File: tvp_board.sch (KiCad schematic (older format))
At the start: 59 parts, among them U1 TVP7002PZP, U4 SN74LVC2G17, U5 AP7361C, U6 TLV70033, U7 NCP703SN19T1G, U9 TLV70019, X1 ACHL-27MHZ-EK, X2 ASEDV-27.000MHZ-LR-T(ECS-2333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

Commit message: update PCB
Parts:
- added D4: RB160M-30TR, custom_components:D_SOD-123_HandSoldering, symbol Device:D_Schottky_ALT
- U5: value AP7361C -> BD33FC0FP; footprint custom_components:SOT-223_Handsoldering -> Package_TO_SOT_SMD:TO-252-2
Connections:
- wire segments 199 -> 203
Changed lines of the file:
@@
 P 10250 3950
 F 0 "U5" H 10250 4200 40  0000 C CNN
-F 1 "AP7361C" H 10250 4150 40  0000 C CNN
-F 2 "custom_components:SOT-223_Handsoldering" H 10250 4050 35  0001 C CIN
+F 1 "BD33FC0FP" H 10250 4150 40  0000 C CNN
+F 2 "Package_TO_SOT_SMD:TO-252-2" H 10250 4050 35  0001 C CIN
 F 3 "" H 10250 3950 60  0000 C CNN
 	1    10250 3950
@@
 	1    0    0    1
 $EndComp
+$Comp
+L Device:D_Schottky_ALT D4
+U 1 1 5FD59D9B
+P 10450 3600
+F 0 "D4" H 10450 3816 50  0000 C CNN
+F 1 "RB160M-30TR" H 10450 3725 50  0000 C CNN
+F 2 "custom_components:D_SOD-123_HandSoldering" H 10450 3600 50  0001 C CNN
+F 3 "~" H 10450 3600 50  0001 C CNN
+	1    10450 3600
+	1    0    0    -1
+$EndComp
+Wire Wire Line
+	10800 3900 10800 3600
+Wire Wire Line
+	10800 3600 10600 3600
+Wire Wire Line
+	10300 3600 9650 3600
+Wire Wire Line
+	9650 3600 9650 3900
 $EndSCHEMATC

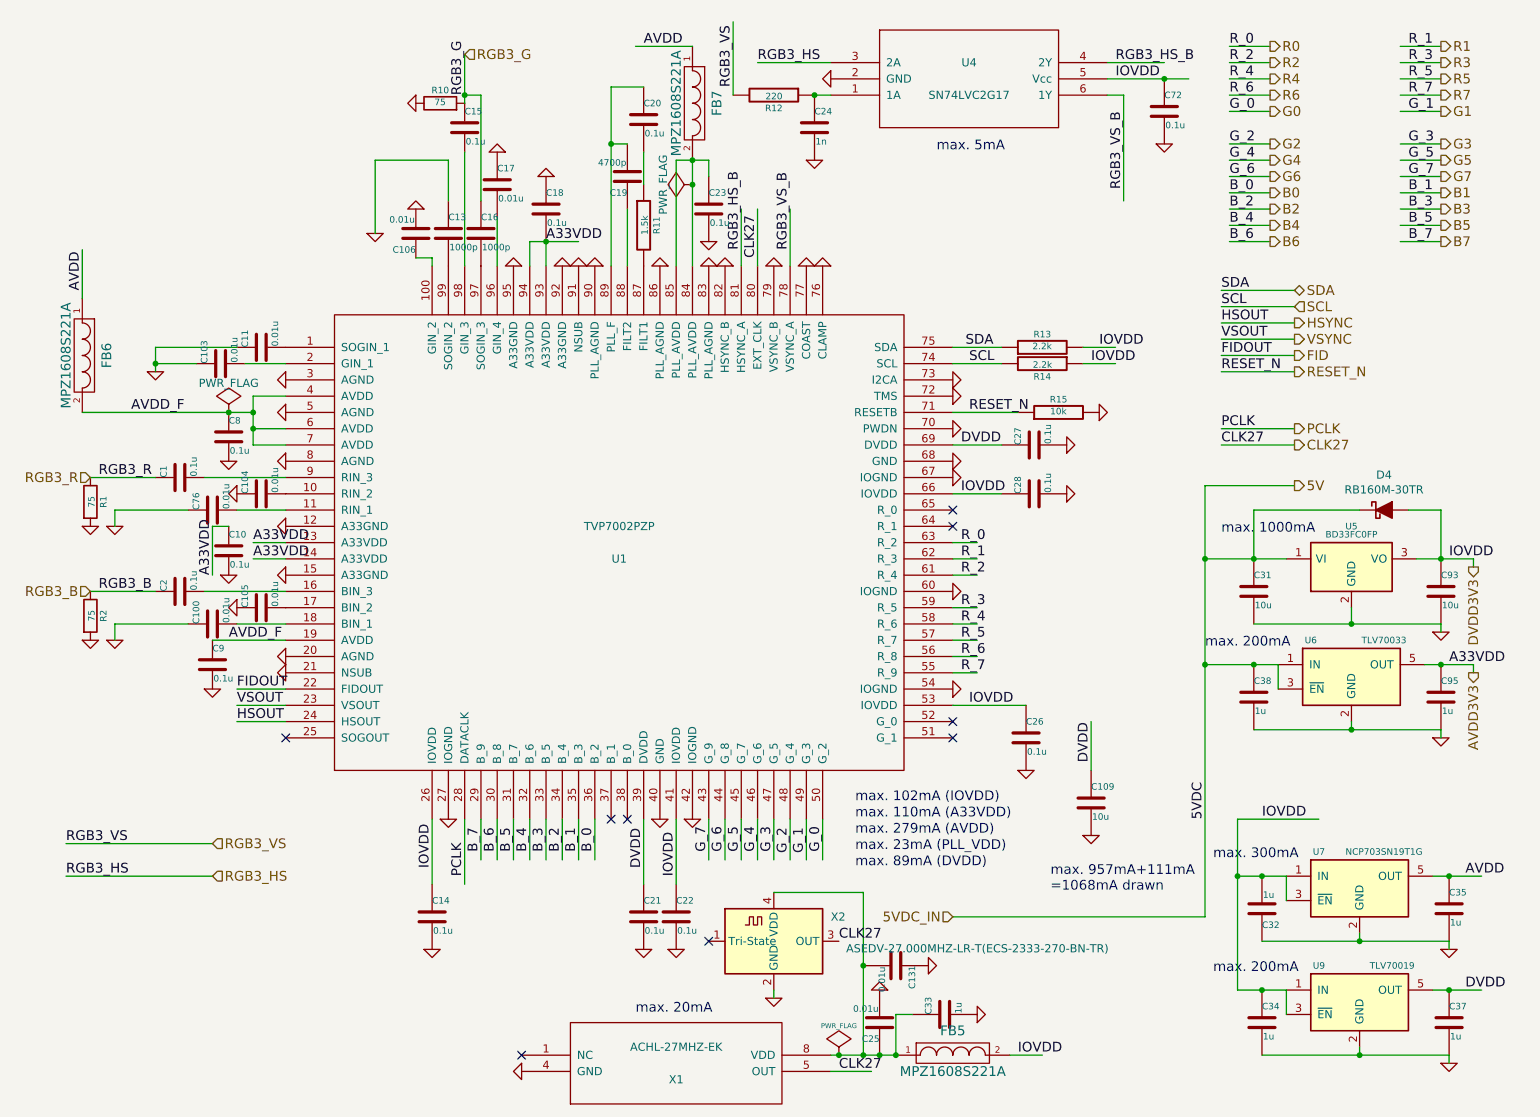
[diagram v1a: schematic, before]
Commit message: update part no
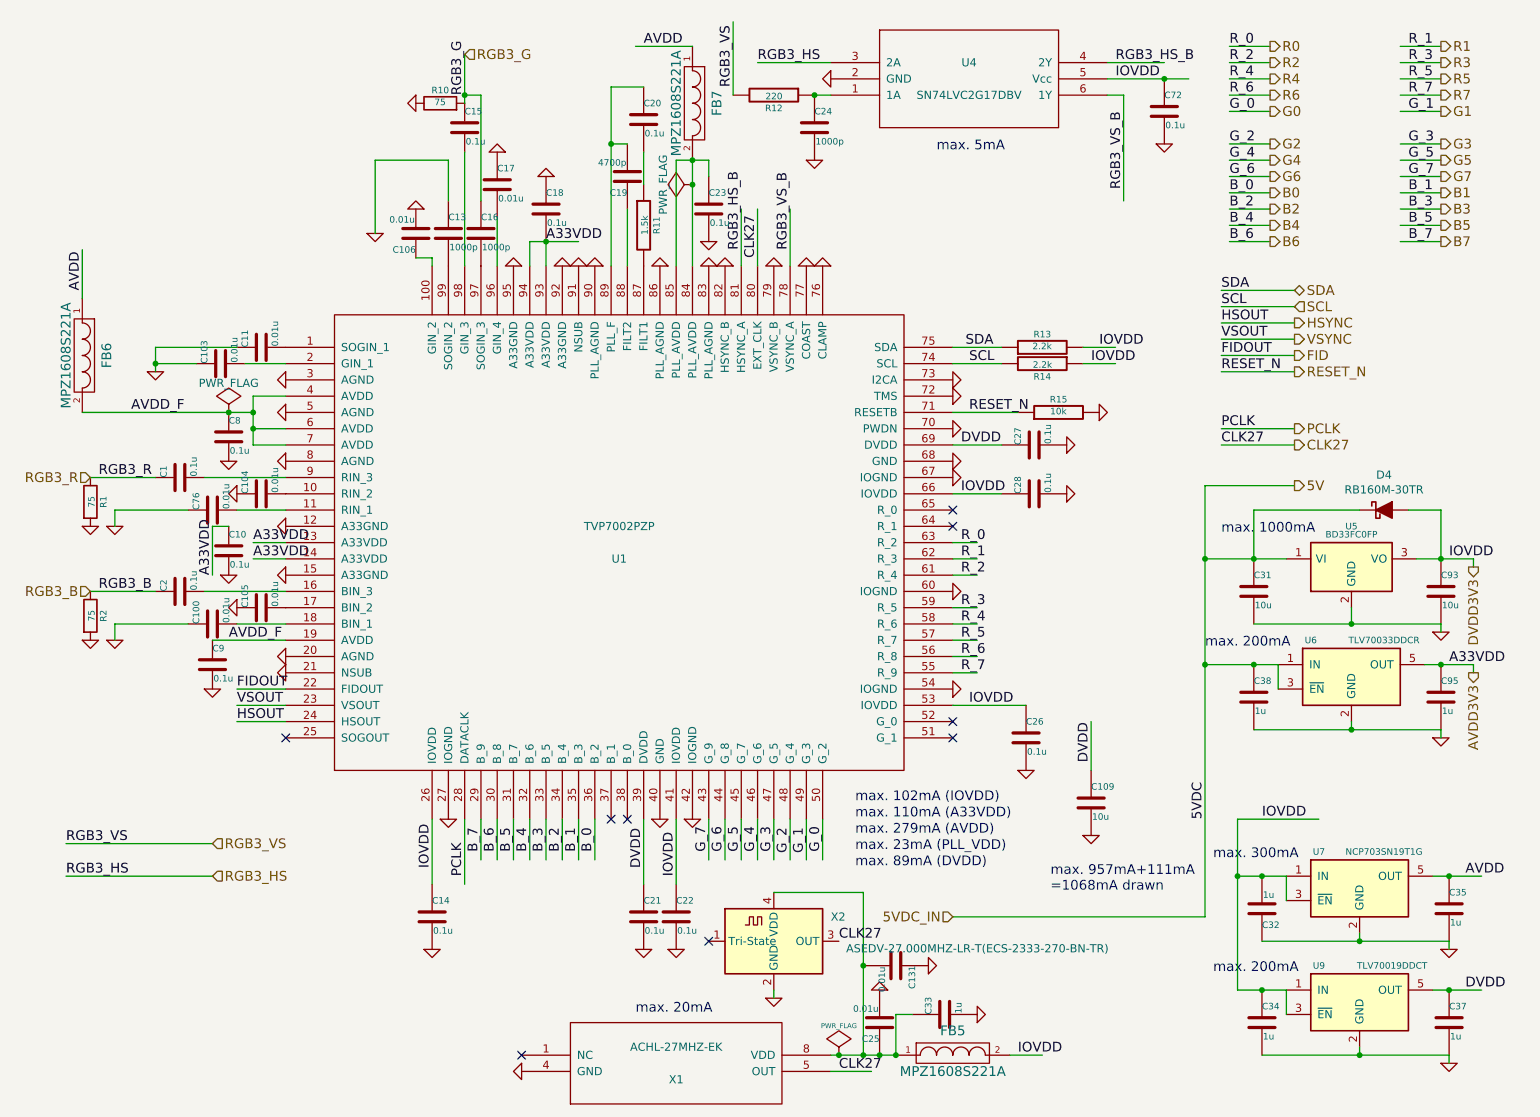
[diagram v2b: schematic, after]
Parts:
- C24: value 1n -> 1000p
- U4: value SN74LVC2G17 -> SN74LVC2G17DBV
- U6: value TLV70033 -> TLV70033DDCR
- U9: value TLV70019 -> TLV70019DDCT
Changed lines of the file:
@@
 AR Path="/54FDD796/53FA4F27" Ref="U9"  Part="1"
 F 0 "U9" H 10050 6800 40  0000 C CNN
-F 1 "TLV70019" H 10500 6800 40  0000 C CNN
+F 1 "TLV70019DDCT" H 10500 6800 40  0000 C CNN
 F 2 "custom_components:SOT-23-5_Handsoldering" H 10300 6700 35  0001 C CIN
 F 3 "" H 10300 6600 60  0000 C CNN
@@
 P 6950 1250
 F 0 "C24" H 6950 1350 40  0000 L CNN
-F 1 "1n" H 6956 1165 40  0000 L CNN
+F 1 "1000p" H 6956 1165 40  0000 L CNN
 F 2 "Capacitor_SMD:C_0603_1608Metric_Pad1.05x0.95mm_HandSolder" H 6988 1100 30  0001 C CNN
 F 3 "~" H 6950 1250 60  0000 C CNN
@@
 AR Path="/54FDD796/5509C1FA" Ref="U6"  Part="1"
 F 0 "U6" H 10000 4800 40  0000 C CNN
-F 1 "TLV70033" H 10450 4800 40  0000 C CNN
+F 1 "TLV70033DDCR" H 10450 4800 40  0000 C CNN
 F 2 "custom_components:SOT-23-5_Handsoldering" H 10250 4700 35  0001 C CIN
 F 3 "" H 10250 4600 60  0000 C CNN
@@
 P 7900 950
 F 0 "U4" H 7900 850 50  0000 C CNN
-F 1 "SN74LVC2G17" H 7900 1050 50  0000 C CNN
+F 1 "SN74LVC2G17DBV" H 7900 1050 50  0000 C CNN
 F 2 "custom_components:SOT-23-6_Handsoldering" H 7900 950 50  0001 C CNN
 F 3 "DOCUMENTATION" H 7900 700 50  0001 C CNN

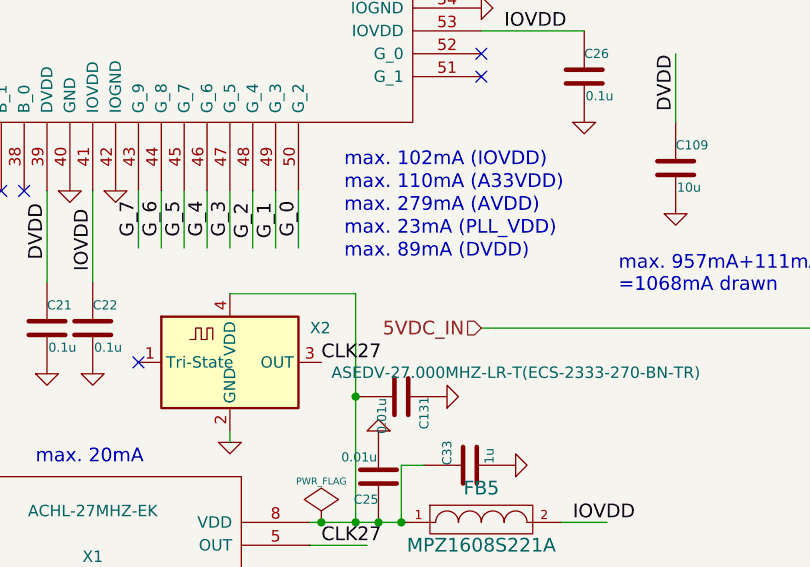
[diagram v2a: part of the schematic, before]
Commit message: add optional components
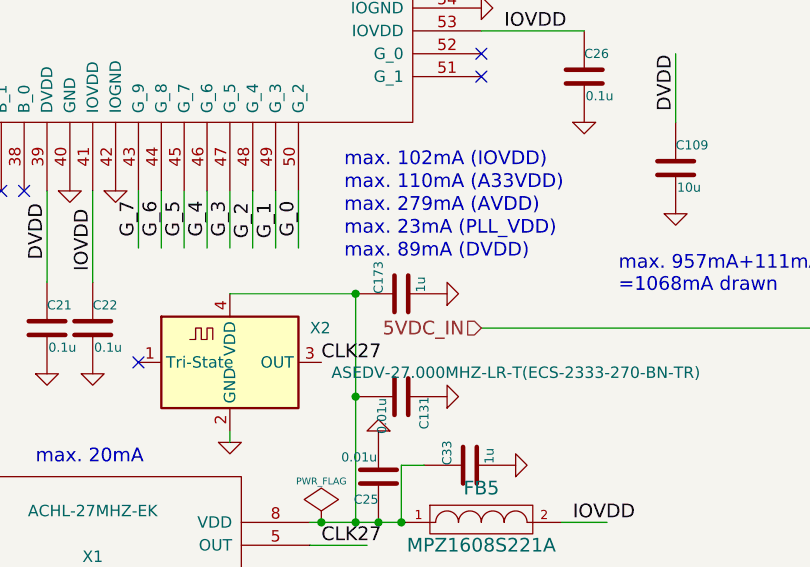
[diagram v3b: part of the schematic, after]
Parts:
- added C173: 1u, Capacitor_SMD:C_0603_1608Metric_Pad1.05x0.95mm_HandSolder, symbol ossc_board-rescue:C-RESCUE-ossc_board
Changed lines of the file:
@@
 Wire Wire Line
 	9650 3600 9650 3900
+$Comp
+L ossc_board-rescue:C-RESCUE-ossc_board C173
+U 1 1 5F4E6F36
+P 7450 5950
+F 0 "C173" H 7450 6050 40  0000 L CNN
+F 1 "1u" H 7456 5865 40  0000 L CNN
+F 2 "Capacitor_SMD:C_0603_1608Metric_Pad1.05x0.95mm_HandSolder" H 7488 5800 30  0001 C CNN
+F 3 "~" H 7450 5950 60  0000 C CNN
+	1    7450 5950
+	0    -1   -1   0
+$EndComp
+Connection ~ 7250 5950
+$Comp
+L ossc_board-rescue:GND-RESCUE-ossc_board #PWR0267
+U 1 1 5F4E73BA
+P 7650 5950
+F 0 "#PWR0267" H 7650 5950 30  0001 C CNN
+F 1 "GND" H 7650 5880 30  0001 C CNN
+F 2 "" H 7650 5950 60  0001 C CNN
+F 3 "" H 7650 5950 60  0000 C CNN
+	1    7650 5950
+	0    -1   -1   0
+$EndComp
 $EndSCHEMATC

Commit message: update values
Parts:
- C11: value 0.01u -> 0.01u (GCM188R72A103KA37J)
- C31: value 10u -> 10u (ZRB18AR61E106ME01L)
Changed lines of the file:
@@
 P 3550 2600
 F 0 "C11" H 3550 2700 40  0000 L CNN
-F 1 "0.01u" H 3556 2515 40  0000 L CNN
+F 1 "0.01u (GCM188R72A103KA37J)" H 3556 2515 40  0000 L CNN
 F 2 "Capacitor_SMD:C_0603_1608Metric_Pad1.05x0.95mm_HandSolder" H 3588 2450 30  0001 C CNN
 F 3 "~" H 3550 2600 60  0000 C CNN
@@
 P 9650 4100
 F 0 "C31" H 9650 4200 40  0000 L CNN
-F 1 "10u" H 9656 4015 40  0000 L CNN
+F 1 "10u (ZRB18AR61E106ME01L)" H 9656 4015 40  0000 L CNN
 F 2 "Capacitor_SMD:C_0603_1608Metric_Pad1.05x0.95mm_HandSolder" H 9688 3950 30  0001 C CNN
 F 3 "~" H 9650 4100 60  0000 C CNN

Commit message: update
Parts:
- removed R13, R14: 2.2k, Resistor_SMD:R_0603_1608Metric_Pad1.05x0.95mm_HandSolder, symbol ossc_board-rescue:R-RESCUE-ossc_board
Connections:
- wire segments 203 -> 201
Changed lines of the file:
@@
 	-1   0    0    1
 $EndComp
-$Comp
-L ossc_board-rescue:R-RESCUE-ossc_board R14
-U 1 1 53FD2BA0
-P 8350 2700
-F 0 "R14" V 8430 2700 40  0000 C CNN
-F 1 "2.2k" V 8357 2701 40  0000 C CNN
-F 2 "Resistor_SMD:R_0603_1608Metric_Pad1.05x0.95mm_HandSolder" V 8280 2700 30  0001 C CNN
-F 3 "~" H 8350 2700 30  0000 C CNN
-	1    8350 2700
-	0    1    1    0
-$EndComp
-$Comp
-L ossc_board-rescue:R-RESCUE-ossc_board R13
-U 1 1 53FD2BB8
-P 8350 2600
-F 0 "R13" V 8430 2600 40  0000 C CNN
-F 1 "2.2k" V 8357 2601 40  0000 C CNN
-F 2 "Resistor_SMD:R_0603_1608Metric_Pad1.05x0.95mm_HandSolder" V 8280 2600 30  0001 C CNN
-F 3 "~" H 8350 2600 30  0000 C CNN
-	1    8350 2600
-	0    -1   -1   0
-$EndComp
-Text Label 8650 2700 0    60   ~ 0
-IOVDD
 Text Label 8050 2600 2    60   ~ 0
 SDA
 Text Label 7900 2700 0    60   ~ 0
 SCL
-Text Label 8700 2600 0    60   ~ 0
-IOVDD
 Text Label 7850 3200 0    60   ~ 0
 DVDD
@@
 	7800 2700 8100 2700
 Wire Wire Line
-	8800 2700 8600 2700
-Wire Wire Line
-	8800 2600 8600 2600
-Wire Wire Line
 	7050 7050 7300 7050

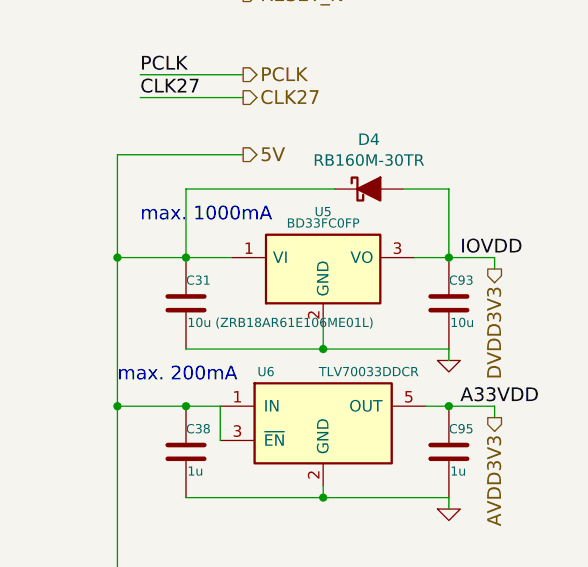
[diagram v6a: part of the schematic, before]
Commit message: change 3.3V liner regulator
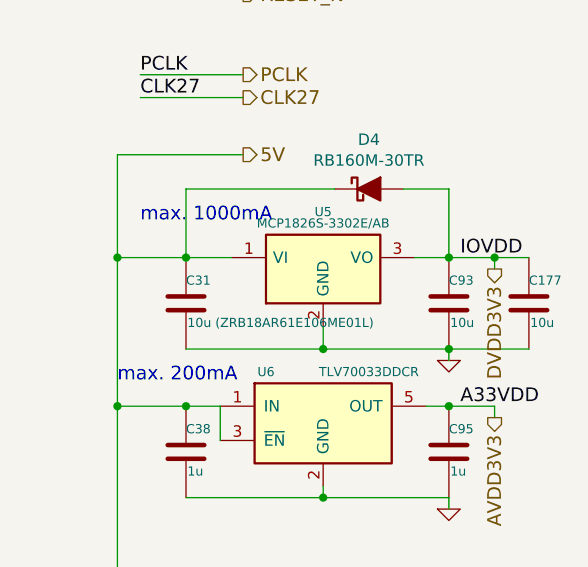
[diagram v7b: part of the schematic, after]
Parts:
- added C177: 10u, Capacitor_SMD:C_0603_1608Metric_Pad1.08x0.95mm_HandSolder, symbol ossc_board-rescue:C-RESCUE-ossc_board
- U5: value BD33FC0FP -> MCP1826S-3302E/AB; footprint Package_TO_SOT_SMD:TO-252-2 -> Package_TO_SOT_THT:TO-220-3_Vertical
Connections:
- wire segments 201 -> 203
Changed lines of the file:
@@
 P 10250 3950
 F 0 "U5" H 10250 4200 40  0000 C CNN
-F 1 "BD33FC0FP" H 10250 4150 40  0000 C CNN
-F 2 "Package_TO_SOT_SMD:TO-252-2" H 10250 4050 35  0001 C CIN
+F 1 "MCP1826S-3302E/AB" H 10250 4150 40  0000 C CNN
+F 2 "Package_TO_SOT_THT:TO-220-3_Vertical" H 10250 4050 35  0001 C CIN
 F 3 "" H 10250 3950 60  0000 C CNN
 	1    10250 3950
@@
 	0    -1   -1   0
 $EndComp
+$Comp
+L ossc_board-rescue:C-RESCUE-ossc_board C177
+U 1 1 60B6062E
+P 11150 4100
+F 0 "C177" H 11150 4200 40  0000 L CNN
+F 1 "10u" H 11156 4015 40  0000 L CNN
+F 2 "Capacitor_SMD:C_0603_1608Metric_Pad1.08x0.95mm_HandSolder" H 11188 3950 30  0001 C CNN
+F 3 "~" H 11150 4100 60  0000 C CNN
+	1    11150 4100
+	1    0    0    -1
+$EndComp
+Wire Wire Line
+	11150 3900 11000 3900
+Connection ~ 11000 3900
+Wire Wire Line
+	11150 4300 10800 4300
+Connection ~ 10800 4300
 $EndSCHEMATC

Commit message: value update
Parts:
- C25: value 0.01u -> (0.01u)
- C33: value 1u -> (1u)
- X1: value ACHL-27MHZ-EK -> (ACHL-27MHZ-EK)
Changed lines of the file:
@@
 AR Path="/54FDD796/53FD28BE" Ref="X1"  Part="1"
 F 0 "X1" H 6100 6900 50  0000 C CNN
-F 1 "ACHL-27MHZ-EK" H 6100 7100 50  0000 C CNN
+F 1 "(ACHL-27MHZ-EK)" H 6100 7100 50  0000 C CNN
 F 2 "custom_components:ACHL-OSC" H 6100 7000 50  0001 C CNN
 F 3 "DOCUMENTATION" H 6100 7000 50  0001 C CNN
@@
 P 7350 6750
 F 0 "C25" H 7350 6850 40  0000 L CNN
-F 1 "0.01u" H 7356 6665 40  0000 L CNN
+F 1 "(0.01u)" H 7356 6665 40  0000 L CNN
 F 2 "Capacitor_SMD:C_0603_1608Metric_Pad1.05x0.95mm_HandSolder" H 7388 6600 30  0001 C CNN
 F 3 "~" H 7350 6750 60  0000 C CNN
@@
 P 7750 6700
 F 0 "C33" H 7750 6800 40  0000 L CNN
-F 1 "1u" H 7756 6615 40  0000 L CNN
+F 1 "(1u)" H 7756 6615 40  0000 L CNN
 F 2 "Capacitor_SMD:C_0603_1608Metric_Pad1.05x0.95mm_HandSolder" H 7788 6550 30  0001 C CNN
 F 3 "~" H 7750 6700 60  0000 C CNN
